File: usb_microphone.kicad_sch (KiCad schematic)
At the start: 0 parts

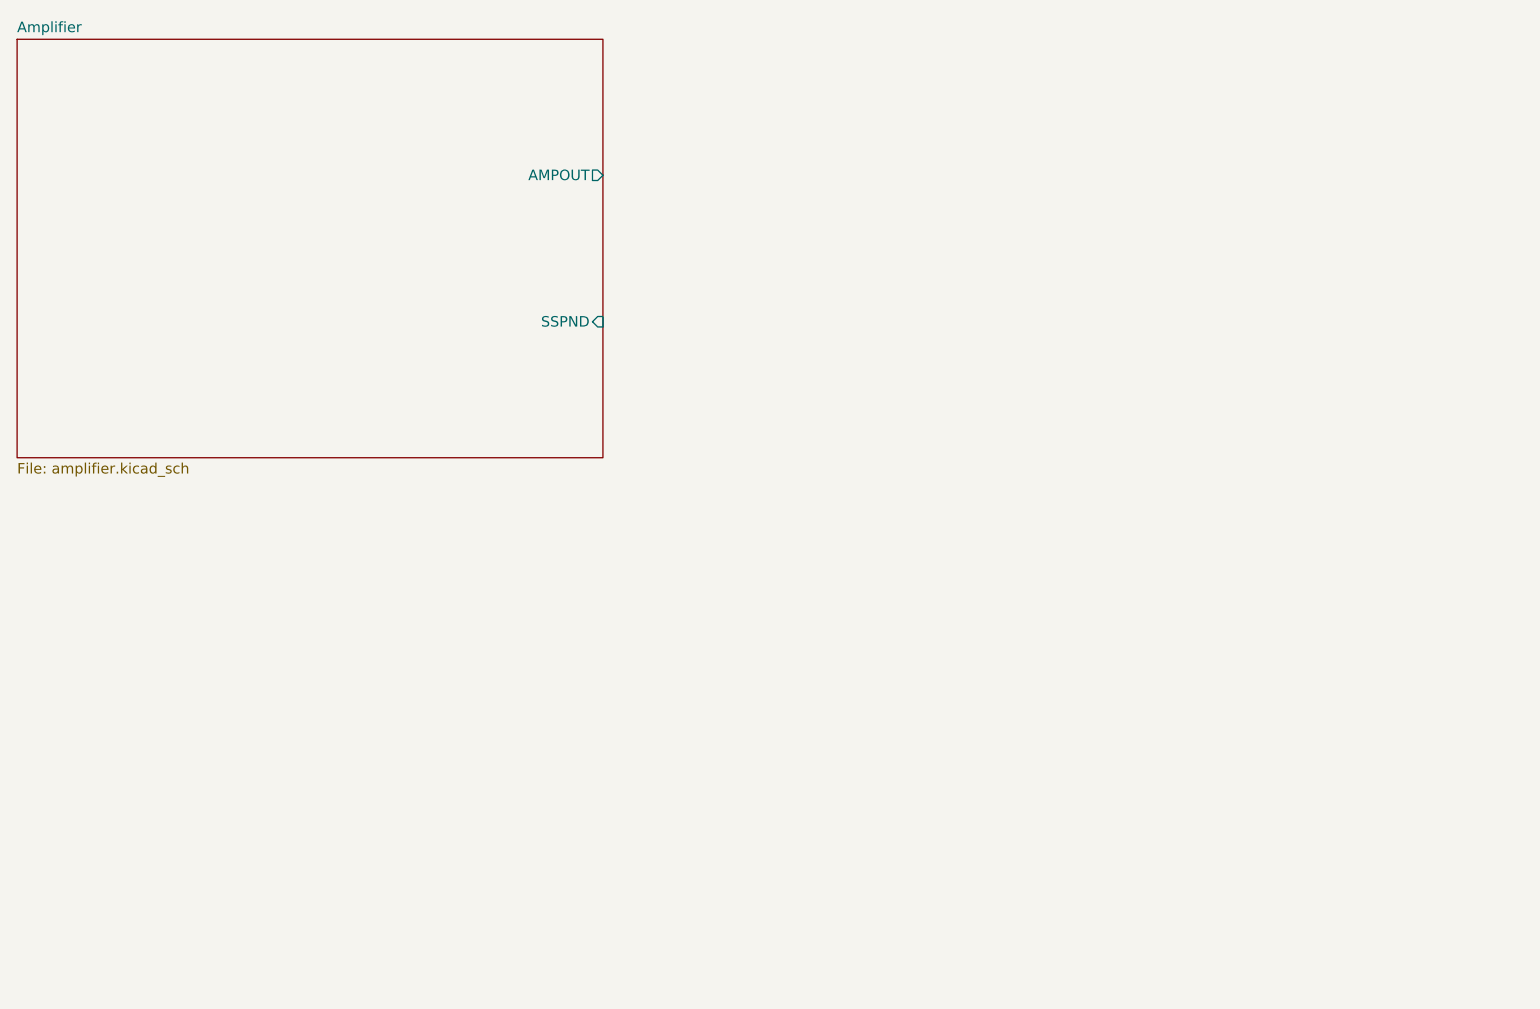
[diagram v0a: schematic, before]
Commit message: Add `Power`, `Connectors` and `Codec`
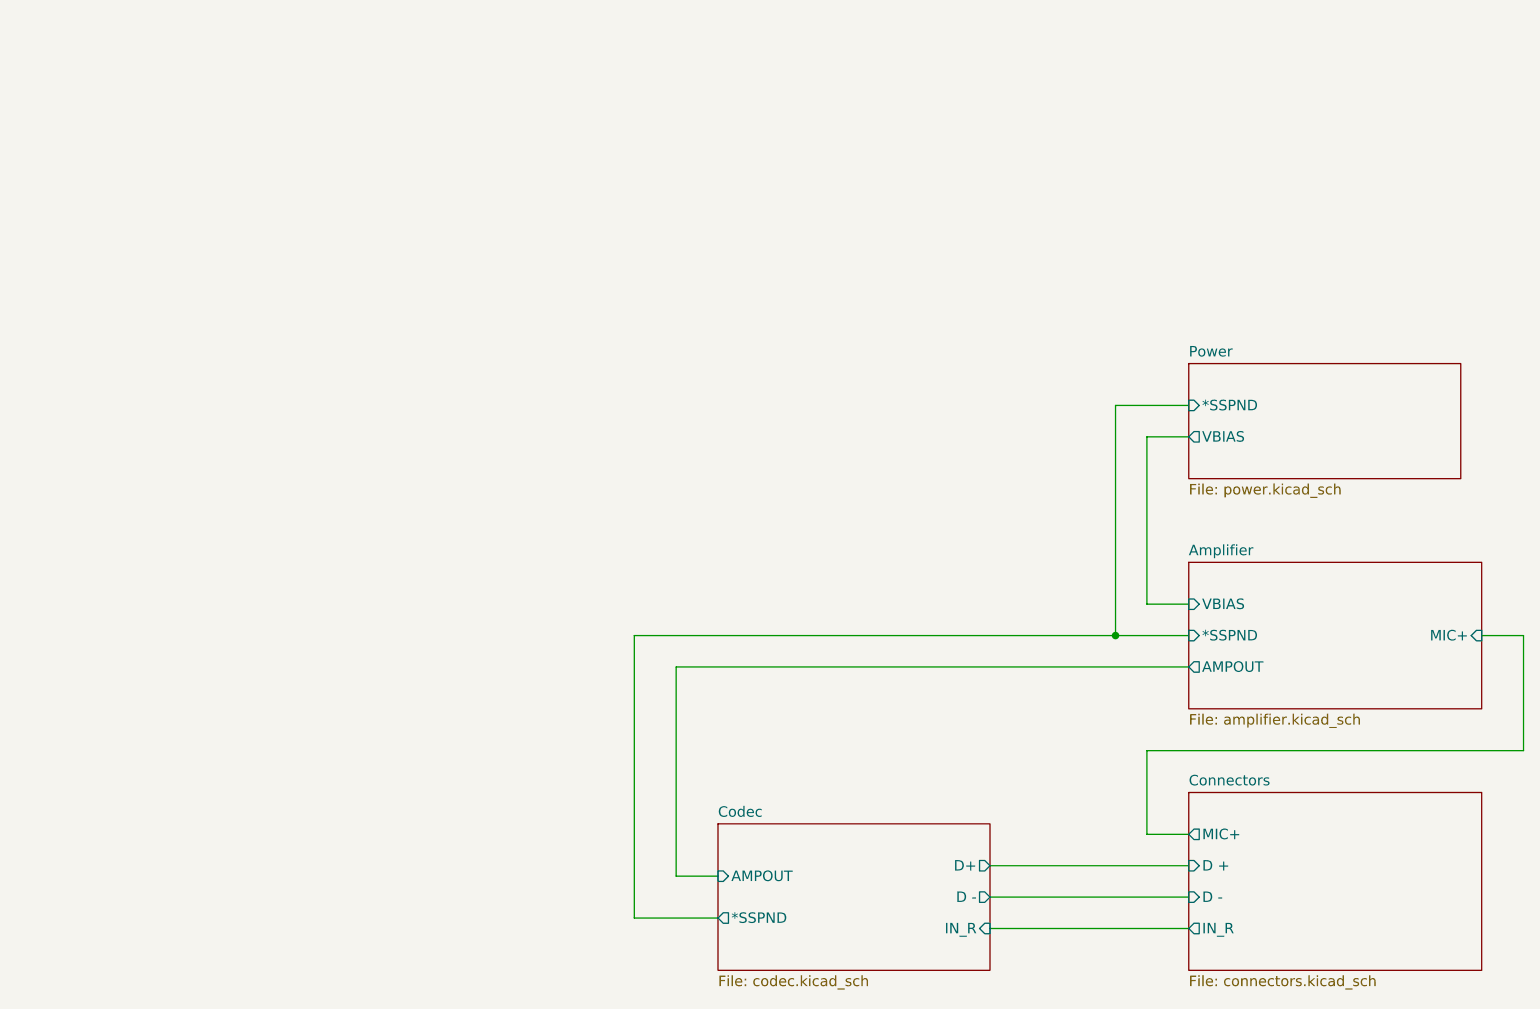
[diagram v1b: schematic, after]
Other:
- added sheet Codec (codec.kicad_sch)
- added sheet Connectors (connectors.kicad_sch)
- added sheet Power (power.kicad_sch)
- sheet Amplifier ports: added *SSPND, MIC+, VBIAS; removed SSPND
